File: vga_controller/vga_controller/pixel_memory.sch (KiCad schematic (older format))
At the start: 0 parts

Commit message: removed interface sheet, combined with pixel_memory
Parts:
- added J?: DB15_Female_HighDensity, symbol Connector:DB15_Female_HighDensity
- added R? (x6): R, symbol Device:R
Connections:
- new net: J?.1, R?.2, R?.2
- new net: J?.2, R?.2, R?.2
- new net: J?.3, R?.2, R?.2
- new net D0: R?.1
- new net D1: R?.1
- new net D2: R?.1
- new net D3: R?.1
- new net D4: R?.1
- new net D5: R?.1
- new net GND: J?.10, J?.5, J?.6, J?.7, J?.8
- new net hsync: J?.13
- new net vsync: J?.14
- no-connect marks 0 -> 13
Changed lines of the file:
@@
 Comment4 ""
 $EndDescr
+$Comp
+L Connector:DB15_Female_HighDensity J?
+U 1 1 5E7935D6
+P 10350 2350
+F 0 "J?" H 10350 3217 50  0000 C CNN
+F 1 "DB15_Female_HighDensity" H 10350 3126 50  0000 C CNN
+F 2 "" H 9400 2750 50  0001 C CNN
+F 3 " ~" H 9400 2750 50  0001 C CNN
+	1    10350 2350
+	1    0    0    -1
+$EndComp
+NoConn ~ 10050 2450
+NoConn ~ 10050 2550
+NoConn ~ 10650 1950
+NoConn ~ 10650 2150
+NoConn ~ 10650 2750
+Text GLabel 10650 2350 2    50   Input ~ 0
+hsync
+Text GLabel 10650 2550 2    50   Input ~ 0
+vsync
+Wire Wire Line
+	10050 1850 9950 1850
+Wire Wire Line
+	9950 1850 9950 2050
+Wire Wire Line
+	9950 2050 10050 2050
+Wire Wire Line
+	9950 2050 9950 2250
+Wire Wire Line
+	9950 2250 10050 2250
+Connection ~ 9950 2050
+Wire Wire Line
+	9950 2250 9950 2650
+Wire Wire Line
+	9950 2650 10050 2650
+Connection ~ 9950 2250
+Wire Wire Line
+	9950 2650 9950 2750
+Wire Wire Line
+	9950 2750 10050 2750
+Connection ~ 9950 2650
+$Comp
+L power:GND #PWR?
+U 1 1 5E794524
+P 9950 2750
+F 0 "#PWR?" H 9950 2500 50  0001 C CNN
+F 1 "GND" H 9955 2577 50  0000 C CNN
+F 2 "" H 9950 2750 50  0001 C CNN
+F 3 "" H 9950 2750 50  0001 C CNN
+	1    9950 2750
+	1    0    0    -1
+$EndComp
+Connection ~ 9950 2750
+$Comp
+L Device:R R?
+U 1 1 5E794C2B
+P 8850 1550
+F 0 "R?" H 8920 1596 50  0000 L CNN
+F 1 "R" H 8920 1505 50  0000 L CNN
+F 2 "" V 8780 1550 50  0001 C CNN
+F 3 "~" H 8850 1550 50  0001 C CNN
+	1    8850 1550
+	1    0    0    -1
+$EndComp
+$Comp
+L Device:R R?
+U 1 1 5E795E91
+P 9100 1550
+F 0 "R?" H 9170 1596 50  0000 L CNN
+F 1 "R" H 9170 1505 50  0000 L CNN
+F 2 "" V 9030 1550 50  0001 C CNN
+F 3 "~" H 9100 1550 50  0001 C CNN
+	1    9100 1550
+	1    0    0    -1
+$EndComp
+$Comp
+L Device:R R?
+U 1 1 5E79630A
+P 8500 1550
+F 0 "R?" H 8570 1596 50  0000 L CNN
+F 1 "R" H 8570 1505 50  0000 L CNN
+F 2 "" V 8430 1550 50  0001 C CNN
+F 3 "~" H 8500 1550 50  0001 C CNN
+	1    8500 1550
+	1    0    0    -1
+$EndComp
+$Comp
+L Device:R R?
+U 1 1 5E796A18
+P 8250 1550
+F 0 "R?" H 8320 1596 50  0000 L CNN
+F 1 "R" H 8320 1505 50  0000 L CNN
+F 2 "" V 8180 1550 50  0001 C CNN
+F 3 "~" H 8250 1550 50  0001 C CNN
+	1    8250 1550
+	1    0    0    -1
+$EndComp
+$Comp
+L Device:R R?
+U 1 1 5E798D48
+P 7650 1550
+F 0 "R?" H 7720 1596 50  0000 L CNN
+F 1 "R" H 7720 1505 50  0000 L CNN
+F 2 "" V 7580 1550 50  0001 C CNN
+F 3 "~" H 7650 1550 50  0001 C CNN
+	1    7650 1550
+	1    0    0    -1
+$EndComp
+$Comp
+L Device:R R?
+U 1 1 5E79939E
+P 7900 1550
+F 0 "R?" H 7970 1596 50  0000 L CNN
+F 1 "R" H 7970 1505 50  0000 L CNN
+F 2 "" V 7830 1550 50  0001 C CNN
+F 3 "~" H 7900 1550 50  0001 C CNN
+	1    7900 1550
+	1    0    0    -1
+$EndComp
+Wire Wire Line
+	8850 1700 9100 1700
+Wire Wire Line
+	8250 1700 8500 1700
+Wire Wire Line
+	7650 1700 7900 1700
+Wire Wire Line
+	9100 1700 9100 1950
+Wire Wire Line
+	9100 1950 10050 1950
+Connection ~ 9100 1700
+Wire Wire Line
+	8500 1700 8500 2150
+Wire Wire Line
+	8500 2150 10050 2150
+Connection ~ 8500 1700
+Wire Wire Line
+	7900 1700 7900 2350
+Wire Wire Line
+	7900 2350 10050 2350
+Connection ~ 7900 1700
+Text GLabel 9100 1400 1    50   Input ~ 0
+D0
+Text GLabel 8850 1400 1    50   Input ~ 0
+D1
+Text GLabel 8500 1400 1    50   Input ~ 0
+D2
+Text GLabel 8250 1400 1    50   Input ~ 0
+D3
+Text GLabel 7900 1400 1    50   Input ~ 0
+D4
+Text GLabel 7650 1400 1    50   Input ~ 0
+D5
+Text GLabel 7700 3200 1    50   Input ~ 0
+D5
+Text GLabel 7850 3200 1    50   Input ~ 0
+D4
+Text GLabel 8000 3200 1    50   Input ~ 0
+D3
+Text GLabel 8150 3200 1    50   Input ~ 0
+D2
+Text GLabel 8300 3200 1    50   Input ~ 0
+D1
+Text GLabel 8450 3200 1    50   Input ~ 0
+D0
+Text GLabel 8600 3200 1    50   Input ~ 0
+hsync
+Text GLabel 8750 3200 1    50   Input ~ 0
+vsync
+NoConn ~ 7700 3200
+NoConn ~ 7850 3200
+NoConn ~ 8000 3200
+NoConn ~ 8150 3200
+NoConn ~ 8300 3200
+NoConn ~ 8450 3200
+NoConn ~ 8600 3200
+NoConn ~ 8750 3200
 $EndSCHEMATC

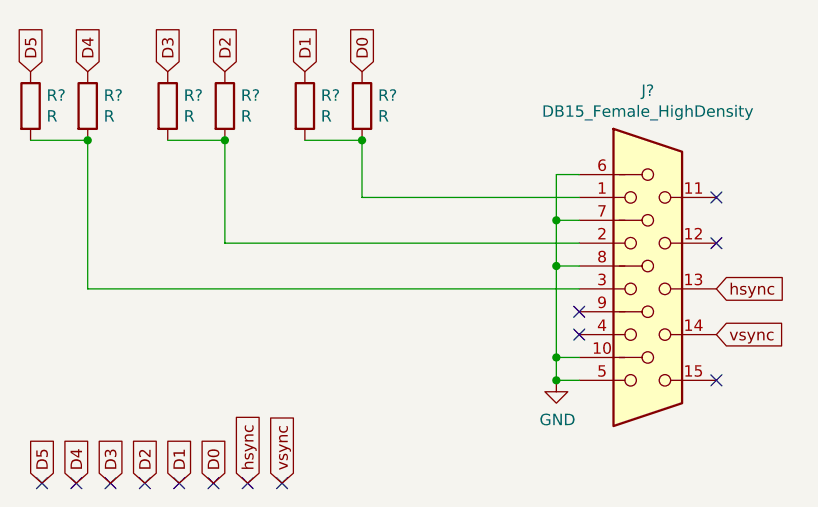
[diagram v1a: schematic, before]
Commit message: removed interface sheet, combined with pixel_memory
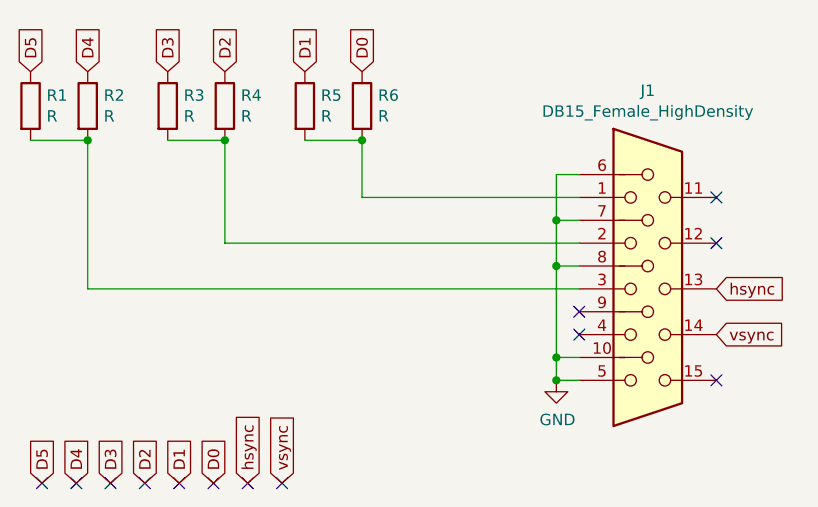
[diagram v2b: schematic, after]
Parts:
- gave numbers to parts that had none: 7
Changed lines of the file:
@@
 $Descr A4 11693 8268
 encoding utf-8
-Sheet 3 5
+Sheet 3 4
 Title "Pixel memory for VGA controller"
 Date ""
@@
 $EndDescr
 $Comp
-L Connector:DB15_Female_HighDensity J?
+L Connector:DB15_Female_HighDensity J1
 U 1 1 5E7935D6
 P 10350 2350
-F 0 "J?" H 10350 3217 50  0000 C CNN
+F 0 "J1" H 10350 3217 50  0000 C CNN
 F 1 "DB15_Female_HighDensity" H 10350 3126 50  0000 C CNN
 F 2 "" H 9400 2750 50  0001 C CNN
@@
 Connection ~ 9950 2650
 $Comp
-L power:GND #PWR?
+L power:GND #PWR01
 U 1 1 5E794524
 P 9950 2750
-F 0 "#PWR?" H 9950 2500 50  0001 C CNN
+F 0 "#PWR01" H 9950 2500 50  0001 C CNN
 F 1 "GND" H 9955 2577 50  0000 C CNN
 F 2 "" H 9950 2750 50  0001 C CNN
@@
 Connection ~ 9950 2750
 $Comp
-L Device:R R?
+L Device:R R5
 U 1 1 5E794C2B
 P 8850 1550
-F 0 "R?" H 8920 1596 50  0000 L CNN
+F 0 "R5" H 8920 1596 50  0000 L CNN
 F 1 "R" H 8920 1505 50  0000 L CNN
 F 2 "" V 8780 1550 50  0001 C CNN
@@
 $EndComp
 $Comp
-L Device:R R?
+L Device:R R6
 U 1 1 5E795E91
 P 9100 1550
-F 0 "R?" H 9170 1596 50  0000 L CNN
+F 0 "R6" H 9170 1596 50  0000 L CNN
 F 1 "R" H 9170 1505 50  0000 L CNN
 F 2 "" V 9030 1550 50  0001 C CNN
@@
 $EndComp
 $Comp
-L Device:R R?
+L Device:R R4
 U 1 1 5E79630A
 P 8500 1550
-F 0 "R?" H 8570 1596 50  0000 L CNN
+F 0 "R4" H 8570 1596 50  0000 L CNN
 F 1 "R" H 8570 1505 50  0000 L CNN
 F 2 "" V 8430 1550 50  0001 C CNN
@@
 $EndComp
 $Comp
-L Device:R R?
+L Device:R R3
 U 1 1 5E796A18
 P 8250 1550
-F 0 "R?" H 8320 1596 50  0000 L CNN
+F 0 "R3" H 8320 1596 50  0000 L CNN
 F 1 "R" H 8320 1505 50  0000 L CNN
 F 2 "" V 8180 1550 50  0001 C CNN
@@
 $EndComp
 $Comp
-L Device:R R?
+L Device:R R1
 U 1 1 5E798D48
 P 7650 1550
-F 0 "R?" H 7720 1596 50  0000 L CNN
+F 0 "R1" H 7720 1596 50  0000 L CNN
 F 1 "R" H 7720 1505 50  0000 L CNN
 F 2 "" V 7580 1550 50  0001 C CNN
@@
 $EndComp
 $Comp
-L Device:R R?
+L Device:R R2
 U 1 1 5E79939E
 P 7900 1550
-F 0 "R?" H 7970 1596 50  0000 L CNN
+F 0 "R2" H 7970 1596 50  0000 L CNN
 F 1 "R" H 7970 1505 50  0000 L CNN
 F 2 "" V 7830 1550 50  0001 C CNN
